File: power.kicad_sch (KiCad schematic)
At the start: 48 parts, among them Q1 DMG1012T-7, Q2 DMG1012T-7, U2 TLV76701_WSON, U3 AP62301_TSOT, U4 AP62301_TSOT

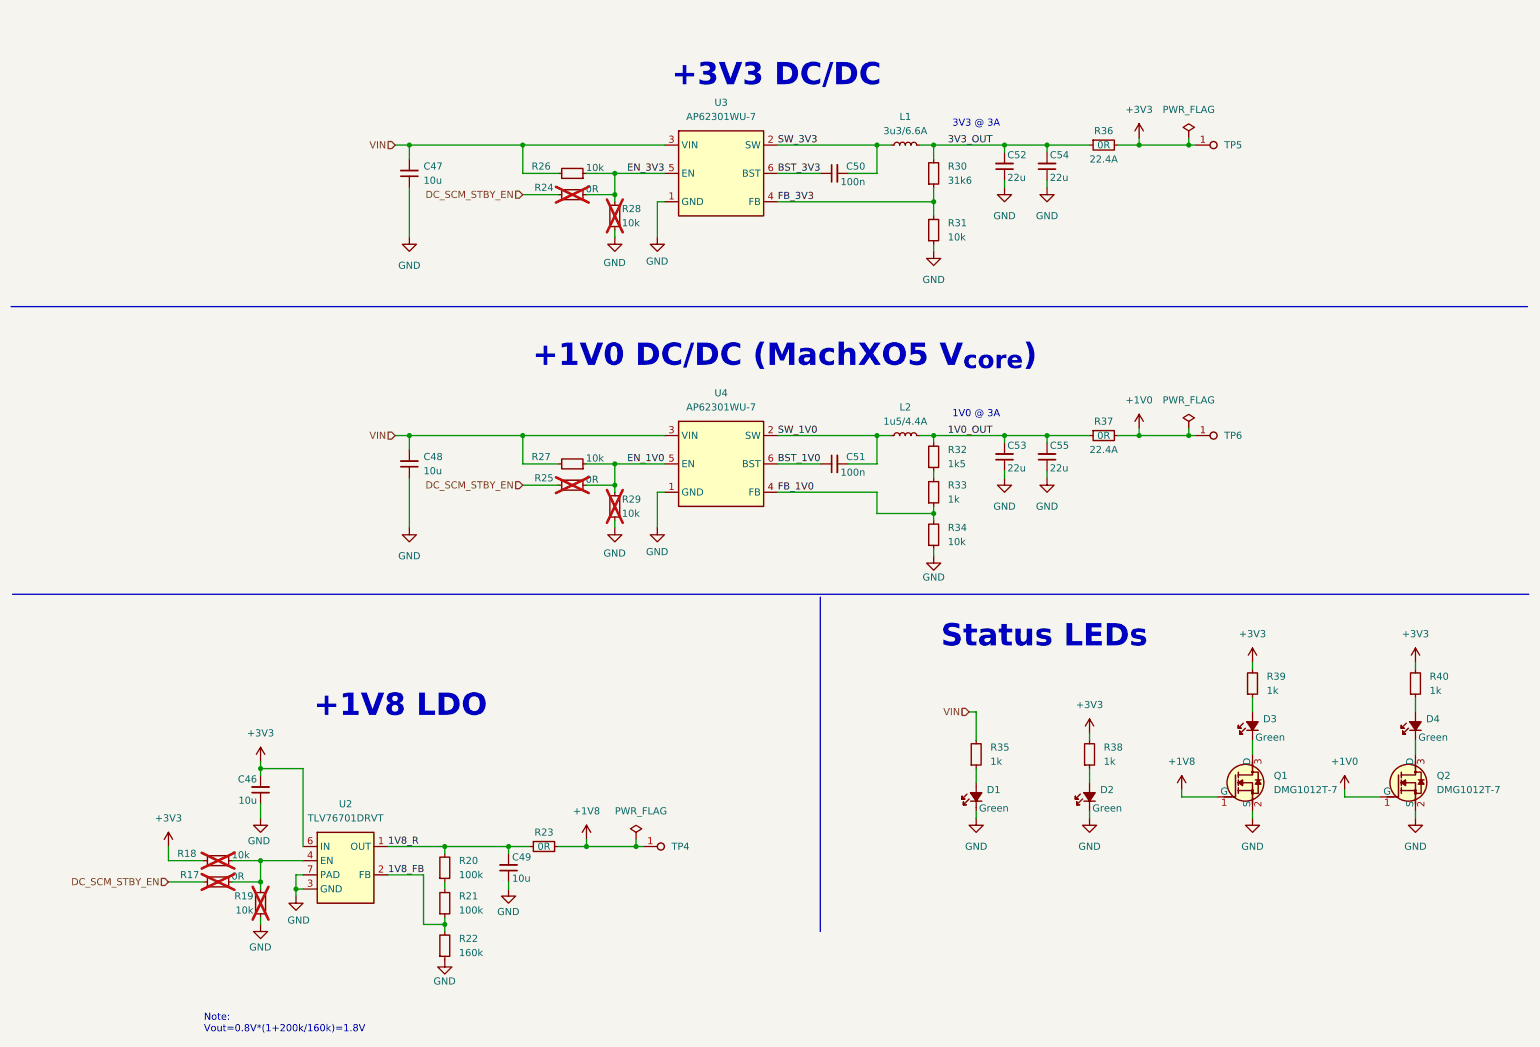
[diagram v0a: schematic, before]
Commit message: [#103953] Sch: Update DCDC
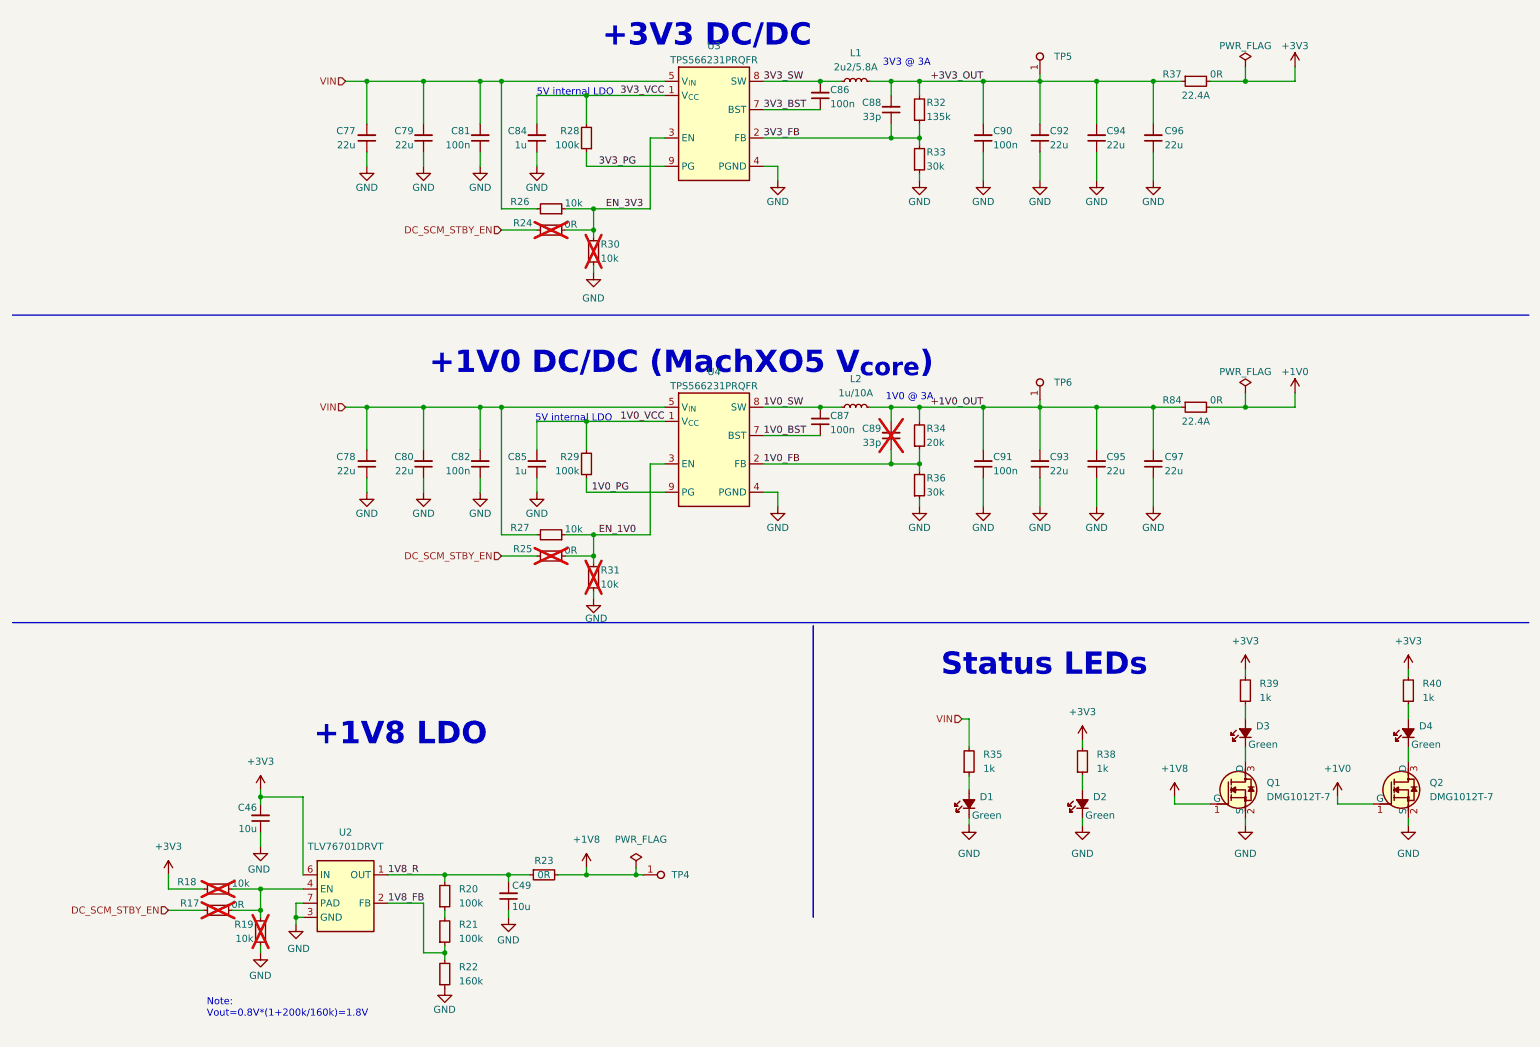
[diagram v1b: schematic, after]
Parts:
- removed C47, C48: C_10u_16V_0603, antmicro-footprints:C_0603_1608Metric, symbol antmicroCapacitors0603:C_10u_16V_0603
- removed C50, C51: C_100n_50V_X8L_0402, antmicro-footprints:C_0402_1005Metric, symbol antmicroCapacitors0402:C_100n_50V_X8L_0402
- removed C52, C53: C_22u_16V_0603, antmicro-footprints:C_0603_1608Metric_EIA, symbol antmicroCapacitors0603:C_22u_16V_0603
- removed C54, C55: C_22u_0603, antmicro-footprints:C_0603_1608Metric, symbol antmicroCapacitors0603:C_22u_0603
- removed L1: L_3u3_6.6A_XEL4030, antmicro-footprints:L_Coilcraft-XEL4030, symbol antmicroFixedInductors:L_3u3_6.6A_XEL4030
- removed L2: L_1u5_4.4A_Bourns-SRP3212A, antmicro-footprints:L_Bourns-SRP3212A, symbol antmicroFixedInductors:L_1u5_4.4A_Bourns-SRP3212A
- removed R30: R_31k6_0402, antmicro-footprints:R_0402_1005Metric, symbol antmicroResistors0402:R_31k6_0402
- removed R31, R34: R_10k_0402, antmicro-footprints:R_0402_1005Metric, symbol antmicroResistors0402:R_10k_0402
- removed R32: R_1k5_0402, antmicro-footprints:R_0402_1005Metric, symbol antmicroResistors0402:R_1k5_0402
- removed R33: R_1k_0402, antmicro-footprints:R_0402_1005Metric, symbol antmicroResistors0402:R_1k_0402
- removed R36: R_0R_22.4A_0603, antmicro-footprints:R_0603_1608Metric, symbol antmicroResistors0603:R_0R_22.4A_0603
- removed U3, U4: AP62301_TSOT, antmicro-footprints:TSOT23-6, symbol antmicroDCDCConverters:AP62301_TSOT
- added C77, C78, C79, C80, C92, C93, C94, C95, C96, C97: C_22u_16V_0603, antmicro-footprints:C_0603_1608Metric_EIA, symbol antmicroCapacitors0603:C_22u_16V_0603
- added C81, C82, C86, C87, C90, C91: C_100n_0402, antmicro-footprints:C_0402_1005Metric, symbol antmicroCapacitors0402:C_100n_0402
- added C84, C85: C_1u_25V_0402, antmicro-footprints:C_0402_1005Metric, symbol antmicroCapacitors0402:C_1u_25V_0402
- added C88, C89: C_33p_0402, antmicro-footprints:C_0402_1005Metric, symbol antmicroCapacitors0402:C_33p_0402
- added L1: L_2u2_5.8A_WE-PMFI-35329222, antmicro-footprints:L_WE-PMFI-353220, symbol antmicroFixedInductors:L_2u2_5.8A_WE-PMFI-35329222
- added L2: L_1u_10A_Bourns-SRP4021HMT, antmicro-footprints:L_Bourns-SRP4021HMT, symbol antmicroFixedInductors:L_1u_10A_Bourns-SRP4021HMT
- added R28, R29: R_100k_0402, antmicro-footprints:R_0402_1005Metric, symbol antmicroResistors0402:R_100k_0402
- added R32: R_135k_0402, antmicro-footprints:R_0402_1005Metric, symbol antmicroResistors0402:R_135k_0402
- added R33, R36: R_30k_0402, antmicro-footprints:R_0402_1005Metric, symbol antmicroResistors0402:R_30k_0402
- added R34: R_20k_0402, antmicro-footprints:R_0402_1005Metric, symbol antmicroResistors0402:R_20k_0402
- added R84: R_0R_22.4A_0603, antmicro-footprints:R_0603_1608Metric, symbol antmicroResistors0603:R_0R_22.4A_0603
- added U3, U4: TPS566231P, antmicro-footprints:VQFN-HR-9_2x1.5mm, symbol antmicroDCDCConverters:TPS566231P
- renumbered R28 to R30, R29 to R31
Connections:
- net +1V0: now also R84.2; no longer R37.2, TP6.1
- net +3V3: now also R37.2; no longer TP5.1
- net EN_1V0: now also U4.3 (EN)
- net EN_3V3: now also U3.3 (EN)
- net GND: now also C77.1, C78.1, C79.1, C80.1, C81.1, C82.1, C84.1, C85.1, C90.1, C91.1, C92.1, C93.1, C94.1, C95.1, C96.1, C97.1, R33.1, R36.1, U3.4 (PGND), U4.4 (PGND)
- net VIN: now also C77.2, C78.2, C79.2, C80.2, C81.2, C82.2, U3.5 (V_{IN}), U3.6 (V_{IN}), U4.5 (V_{IN}), U4.6 (V_{IN})
- net 1V0_OUT renamed +3V3_OUT
- net +3V3_OUT: now also TP5.1, C88.2, C90.2, C92.2, C94.2, C96.2, L1.2, R32.2
- new net +1V0_OUT: C89.2, C91.2, C93.2, C95.2, C97.2, L2.2, R34.2, R84.1, TP6.1
- new net 1V0_BST: C87.1, U4.7 (BST)
- new net 1V0_FB: C89.1, R34.1, R36.2, U4.2 (FB)
- new net 1V0_PG: R29.1, U4.9 (PG)
- new net 1V0_SW: C87.2, L2.1, U4.8 (SW)
- new net 1V0_VCC: C85.2, R29.2, U4.1 (V_{CC})
- new net 3V3_BST: C86.1, U3.7 (BST)
- new net 3V3_FB: C88.1, R32.1, R33.2, U3.2 (FB)
- new net 3V3_PG: R28.1, U3.9 (PG)
- new net 3V3_SW: C86.2, L1.1, U3.8 (SW)
- new net 3V3_VCC: C84.2, R28.2, U3.1 (V_{CC})
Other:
- note added: "5V internal LDO"
- moved on the sheet: C46, C49, D1, D2, D3, D4, Q1, Q2, R17, R18, R19, R20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
